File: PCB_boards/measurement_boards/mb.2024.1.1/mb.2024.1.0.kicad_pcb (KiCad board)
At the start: 2 copper layers, 247.8 x 124.2 mm, 120 parts, among them J1 DPS_out_12v_GND, J10 DPS+, J11 Screw_Terminal_VMN, J12 Conn_01x08_Socket, J13 Connector_I2C_for_mux, J14 Conn_01x02_Socket, J15 Conn_01x08_Socket, J16 RX_bat, J17 DPS GND, J18 ELEC_M, J19 ELEC_N, J2 DPS5005_input_0_to_50V, J20 shunt +, J21 shunt -, J22 Conn_01x04_Socket, J23 Conn_01x05_Socket, J24 Connector_I2C_for_MC, J25 Conn_01x04_Socket, J26 Conn_01x05_Socket, J27 Screw_Terminal_01x03, J3 Screw_Terminal_AB, J4 Conn_01x08_Socket, J5 Conn_01x04_Socket, J6 Conn_01x08_Socket, J7 Raspberry_Pi_2_3, J8 Connector_I2C_for_MCP23008, J9 TX_bat, K1 G5LE-1, K2 G5LE-1, K3 G5LE-1, K4 G5LE-1, K5 G5LE-1, K6 G5LE-1, K7 G5LE-1, Q1 ZVN4206ASTZ, Q2 ZVN4206ASTZ, Q3 ZVN4206ASTZ, Q4 ZVN4206ASTZ, Q5 ZVN4206ASTZ, Q6 ZVN4206ASTZ, Q7 ZVN4206ASTZ, U1 MCP23008-xP, U10 DG411xJ, U2 OP07, U4 1085, U5 1085, U6 OP07, U7 REF03GP, U8 MCP23008-xP, U9 OP07

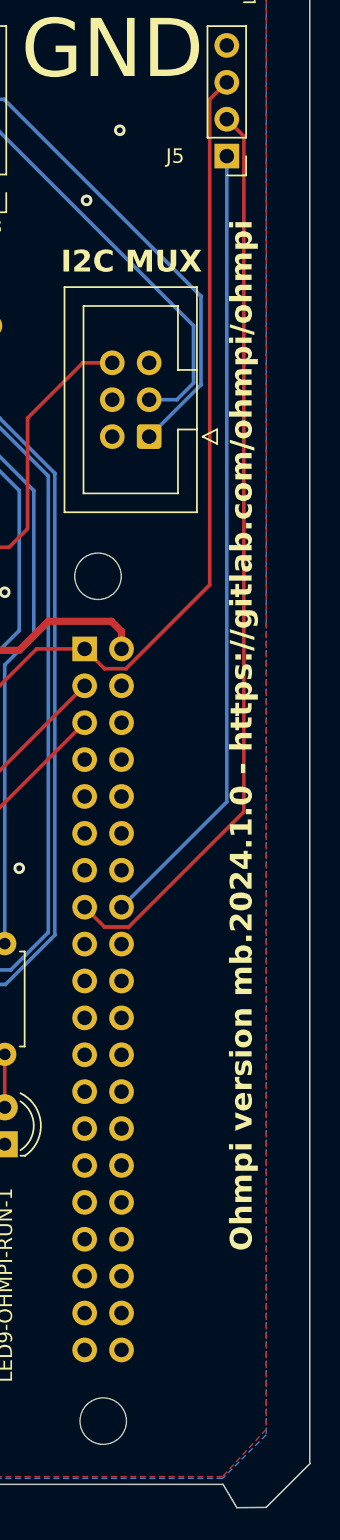
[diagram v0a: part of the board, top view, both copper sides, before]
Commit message: update version number on the PCB
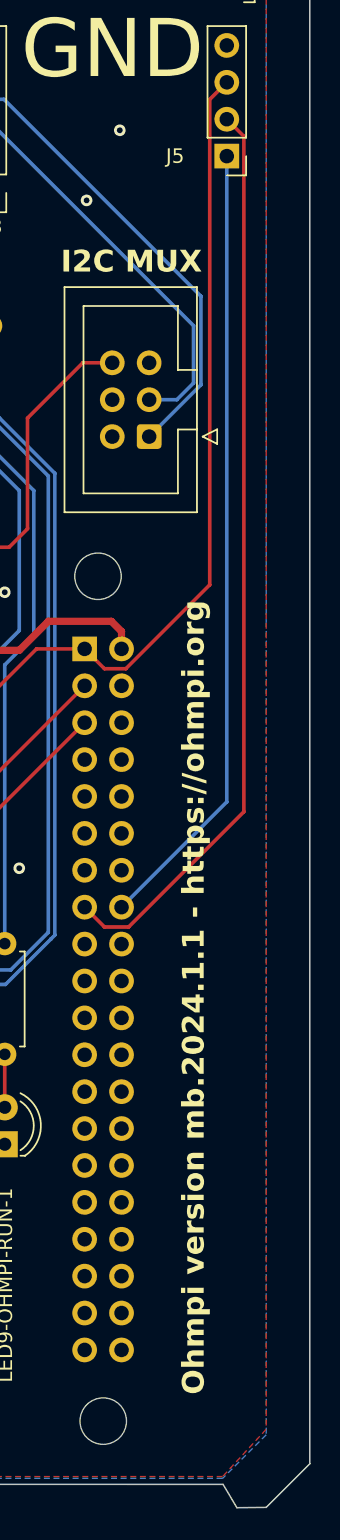
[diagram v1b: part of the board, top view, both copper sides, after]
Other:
- board text added: "Ohmpi version mb.2024.1.1 - https://ohmpi.org"
- board text removed: "Ohmpi version mb.2024.1.0 - https://gitlab.com/ohmpi/ohmpi"
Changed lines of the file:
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@@
 		)
 	)
-	(gr_text "Ohmpi version mb.2024.1.0 - https://gitlab.com/ohmpi/ohmpi"
-		(at 257.302 101.854 90)
+	(gr_text "Ohmpi version mb.2024.1.1 - https://ohmpi.org"
+		(at 254 119.888 90)
 		(layer "F.SilkS")
 		(effects
